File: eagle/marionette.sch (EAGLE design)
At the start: 483 parts, among them J12 IDC_RECEPTACLE_20PIN-S9172-ND, J13 CONN_HEADER_JTAG, J2 SP3T Jumper Switch, J22 ZX62D-B-5P8, J3 IDC_RECEPTACLE_2X20-S9175-ND, J5 CON_COAX_PWR_PJ-047AH-NO_MILL, J8 IDC_RECEPTACLE_2X20-S9175-ND, J9 IDC_RECEPTACLE_2X20-S9175-ND, M5002 IRFR9024NTRPBF, Q2 NFET_DUAL_DMN63D8LDW, Q3 AO3419, SW1 SW-MOM-TACTILE-B3F-1000, SW2 SW-MOM-TACTILE-B3F-1000, U1 SWITCH_74HC4066D, U10 LMV344, U11 STM32F427-STM32F427, U13 CON_HIROSE_DM3D(MICROSD), U14 USB3320, U15 SWITCH_74HC4066D, U17 LM3671, U2 FR014H5JZ, U3 MIC5305_MIC5305-3.3YD5, U4 DAC124S085CIMM, U40 MIC5305_MIC5305-3.3YD5, U41 MIC5305-MIC5305-1.8YD5, U5 MAX3051ESAESA+, U5002 TPS40200, U6 OPAMP_DUAL_MC4558CDT, U7 LMV344, U8 LMV344, U9 LMV344, X1 ABSO7

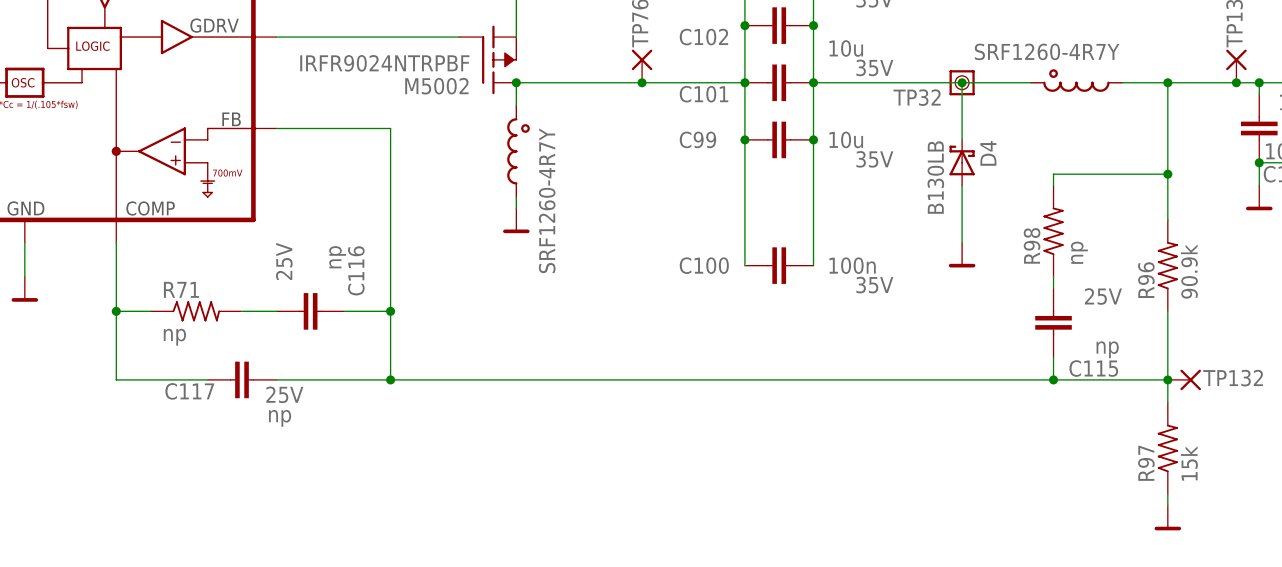
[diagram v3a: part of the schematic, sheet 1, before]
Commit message: Added compensation values to the marionette zeta.
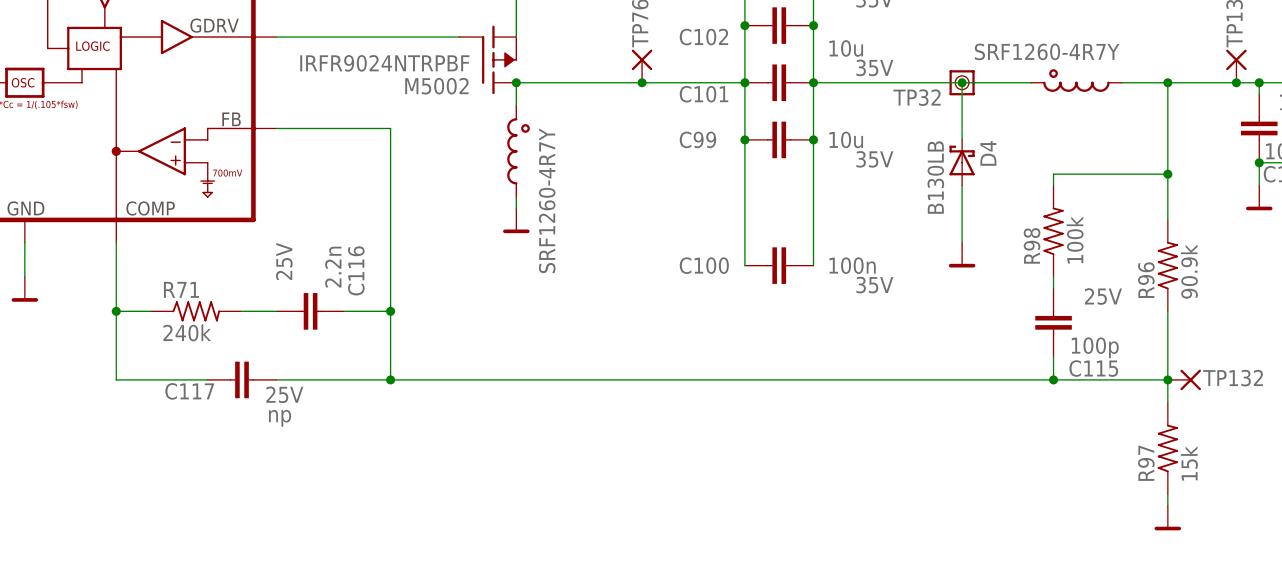
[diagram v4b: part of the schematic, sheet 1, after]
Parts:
- C115: value np -> 100p
- C116: value np -> 2.2n
- R71: value np -> 240k
- R98: value np -> 100k
- renumbered R1 to R201, R2 to R202, R3 to R203, R4 to R204
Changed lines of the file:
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@@
 <setting verticaltext="up"/>
 </settings>
-<grid distance="0.05" unitdist="inch" unit="inch" style="lines" multiple="2" display="no" altdistance="0.01" altunitdist="inch" altunit="inch"/>
+<grid distance="0.1" unitdist="inch" unit="inch" style="lines" multiple="1" display="no" altdistance="0.01" altunitdist="inch" altunit="inch"/>
 <layers>
 <layer number="1" name="Top" color="4" fill="1" visible="no" active="no"/>
@@
 <attribute name="V_RATING" value="10V"/>
 </part>
-<part name="R1" library="rcl_custom" deviceset="R-US_" device="0402-B" value="8.06k"/>
+<part name="R201" library="rcl_custom" deviceset="R-US_" device="0402-B" value="8.06k"/>
 <part name="C29" library="rcl_custom" deviceset="C-EU" device="0402-B" value="10n">
 <attribute name="V_RATING" value="10V"/>
@@
 <part name="GND3" library="GROUND" deviceset="GND" device=""/>
 <part name="J22" library="con-hirose-microusb" deviceset="ZX62D-B-5P8" device=""/>
-<part name="R2" library="rcl_custom" deviceset="R-US_" device="0402-B" value="4.7k"/>
-<part name="R3" library="rcl_custom" deviceset="R-US_" device="0402-B" value="4.7k"/>
+<part name="R202" library="rcl_custom" deviceset="R-US_" device="0402-B" value="4.7k"/>
+<part name="R203" library="rcl_custom" deviceset="R-US_" device="0402-B" value="4.7k"/>
 <part name="R6" library="rcl_custom" deviceset="R-US_" device="0402-B" value="4.7k"/>
 <part name="R7" library="rcl_custom" deviceset="R-US_" device="0402-B" value="4.7k"/>
@@
 <part name="TP119" library="marionette" deviceset="PAD+X" device="-0.7-NO_CREAM+SILK"/>
 <part name="TP120" library="marionette" deviceset="PAD+X" device="-0.7-NO_CREAM+SILK"/>
-<part name="R4" library="rcl_custom" deviceset="R-US_" device="0402-B" value="1Meg"/>
+<part name="R204" library="rcl_custom" deviceset="R-US_" device="0402-B" value="1Meg"/>
 <part name="C28" library="rcl_custom" deviceset="C-EU" device="0402-B" value="1u">
 <attribute name="V_RATING" value="10V"/>
@@
 <attribute name="V_RATING" value="10V"/>
 </part>
-<part name="C115" library="rcl_custom" deviceset="C-EU" device="0402-B" value="np">
+<part name="C115" library="rcl_custom" deviceset="C-EU" device="0402-B" value="100p">
 <attribute name="V_RATING" value="25V"/>
 </part>
-<part name="C116" library="rcl_custom" deviceset="C-EU" device="0402-B" value="np">
+<part name="C116" library="rcl_custom" deviceset="C-EU" device="0402-B" value="2.2n">
 <attribute name="V_RATING" value="25V"/>
 </part>
@@
 <part name="SW2" library="marionette" deviceset="SW-MOM-TACTILE" device="-B3F-1000"/>
 <part name="J5" library="marionette" deviceset="CON_COAX_PWR_PJ-047AH" device="-NO_MILL"/>
-<part name="R71" library="rcl_custom" deviceset="R-US_" device="0402-B" value="np"/>
+<part name="R71" library="rcl_custom" deviceset="R-US_" device="0402-B" value="240k"/>
 <part name="R96" library="rcl_custom" deviceset="R-US_" device="0402-B" value="90.9k"/>
 <part name="R97" library="rcl_custom" deviceset="R-US_" device="0402-B" value="15k"/>
-<part name="R98" library="rcl_custom" deviceset="R-US_" device="0402-B" value="np"/>
+<part name="R98" library="rcl_custom" deviceset="R-US_" device="0402-B" value="100k"/>
 <part name="C144" library="rcl_custom" deviceset="C-EU" device="0402-B" value="100p">
 <attribute name="V_RATING" value="50V"/>
@@
 </plain>
 <instances>
-<instance part="R1" gate="R" x="523.24" y="736.6" rot="R270"/>
+<instance part="R201" gate="R" x="523.24" y="736.6" rot="R270"/>
 <instance part="C29" gate="CE" x="427.99" y="803.91" smashed="yes">
 <attribute name="V_RATING" x="429.26" y="798.83" size="1.778" layer="96"/>
@@
 <instance part="FRAME1" gate="G$1" x="558.8" y="50.8"/>
 <instance part="FRAME1" gate="G$2" x="1010.92" y="0"/>
-<instance part="R2" gate="R" x="213.36" y="466.09" rot="R90"/>
-<instance part="R3" gate="R" x="226.06" y="466.09" rot="R90"/>
+<instance part="R202" gate="R" x="213.36" y="466.09" rot="R90"/>
+<instance part="R203" gate="R" x="226.06" y="466.09" rot="R90"/>
 <instance part="C34" gate="CE" x="251.46" y="350.52" smashed="yes" rot="R90">
 <attribute name="V_RATING" x="247.65" y="345.44" size="1.778" layer="96"/>
@@
 <attribute name="VALUE" x="247.142" y="26.543" size="0.762" layer="96" rot="R90"/>
 </instance>
-<instance part="R4" gate="R" x="646.43" y="742.95" smashed="yes" rot="R270">
+<instance part="R204" gate="R" x="646.43" y="742.95" smashed="yes" rot="R270">
 <attribute name="NAME" x="644.9314" y="736.6" size="1.778" layer="95" rot="R90"/>
 <attribute name="VALUE" x="643.128" y="749.3" size="1.778" layer="96" rot="R270"/>
@@
 <wire x1="641.35" y1="735.33" x2="646.43" y2="735.33" width="0.1524" layer="91"/>
 <junction x="652.78" y="735.33"/>
-<pinref part="R4" gate="R" pin="2"/>
+<pinref part="R204" gate="R" pin="2"/>
 <wire x1="646.43" y1="735.33" x2="652.78" y2="735.33" width="0.1524" layer="91"/>
 <wire x1="646.43" y1="735.33" x2="646.43" y2="737.87" width="0.1524" layer="91"/>
@@
 </segment>
 <segment>
-<pinref part="R1" gate="R" pin="2"/>
+<pinref part="R201" gate="R" pin="2"/>
 <wire x1="523.24" y1="731.52" x2="523.24" y2="730.25" width="0.1524" layer="91"/>
 <wire x1="523.24" y1="730.25" x2="525.78" y2="730.25" width="0.1524" layer="91"/>
@@
 <wire x1="652.78" y1="749.3" x2="652.78" y2="746.76" width="0.1524" layer="91"/>
 <junction x="652.78" y="749.3"/>
-<pinref part="R4" gate="R" pin="1"/>
+<pinref part="R204" gate="R" pin="1"/>
 <wire x1="646.43" y1="748.03" x2="646.43" y2="749.3" width="0.1524" layer="91"/>
 <wire x1="646.43" y1="749.3" x2="652.78" y2="749.3" width="0.1524" layer="91"/>
@@
 <segment>
 <pinref part="U14" gate="U" pin="RBIAS"/>
-<pinref part="R1" gate="R" pin="1"/>
+<pinref part="R201" gate="R" pin="1"/>
 <wire x1="523.24" y1="744.22" x2="523.24" y2="742.95" width="0.1524" layer="91"/>
 <pinref part="TP21" gate="TP" pin="P"/>
@@
 <wire x1="252.73" y1="459.74" x2="236.22" y2="459.74" width="0.1524" layer="91"/>
 <label x="132.08" y="459.74" size="1.778" layer="95" font="vector"/>
-<pinref part="R2" gate="R" pin="1"/>
+<pinref part="R202" gate="R" pin="1"/>
 <wire x1="236.22" y1="459.74" x2="213.36" y2="459.74" width="0.1524" layer="91"/>
 <wire x1="213.36" y1="459.74" x2="104.14" y2="459.74" width="0.1524" layer="91"/>
@@
 <wire x1="226.06" y1="454.66" x2="226.06" y2="461.01" width="0.1524" layer="91"/>
 <junction x="226.06" y="454.66"/>
-<pinref part="R3" gate="R" pin="1"/>
+<pinref part="R203" gate="R" pin="1"/>
 <pinref part="U11" gate="G6" pin="PF1"/>
 <pinref part="TP46" gate="TP" pin="P"/>
@@
 </segment>
 <segment>
-<pinref part="R2" gate="R" pin="2"/>
+<pinref part="R202" gate="R" pin="2"/>
 <wire x1="213.36" y1="471.17" x2="213.36" y2="472.44" width="0.1524" layer="91"/>
 <wire x1="213.36" y1="472.44" x2="226.06" y2="472.44" width="0.1524" layer="91"/>
-<pinref part="R3" gate="R" pin="2"/>
+<pinref part="R203" gate="R" pin="2"/>
 <wire x1="226.06" y1="472.44" x2="226.06" y2="471.17" width="0.1524" layer="91"/>
 <wire x1="226.06" y1="472.44" x2="226.06" y2="473.71" width="0.1524" layer="91"/>

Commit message: Added some datasheets and made some notes to the marionette.sch and marionette.brd
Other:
- note added: "Add power supply indicator lights, i.e. 5V, 3.3V_digital, 3.3V_analog, etc."
- note added: "Add some package details to MAX3051 SO-8 package: tplace layer demarcation of pin 1 Digikey part no. in the device info."
- note added: "This RGB LED is WAYYYY too small - get bigger package."
- note added: "Use ADP160AUJZ-1.8"
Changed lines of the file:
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@@
 <text x="1101.09" y="5.08" size="5.08" layer="94">2.0</text>
 <text x="1026.16" y="24.13" size="7.62" layer="94">POWER</text>
-<text x="861.06" y="276.86" size="7.62" layer="112">MIC5305 fixed regulators are non-stocked at Mouser and Digikey.  Also their accuracy is only 1%, so this was stupid choice.  Should use adjustable regulators for BOM reduction in future.</text>
-<text x="862.33" y="261.62" size="7.62" layer="112">Temporary fix for V2.0 is using the ADP121 1% LDO from Analog.</text>
+<text x="792.48" y="320.04" size="7.62" layer="112">MIC5305 fixed regulators are non-stocked at Mouser and Digikey.  Also their accuracy is only 1%, so this was stupid choice.  Should use adjustable regulators for BOM reduction in future.</text>
+<text x="791.21" y="304.8" size="7.62" layer="112">Temporary fix for V2.0 is using the ADP121 1% LDO from Analog.</text>
+<text x="726.44" y="236.22" size="1.778" layer="112">Use ADP160AUJZ-1.8</text>
+<text x="792.48" y="292.1" size="7.62" layer="112">Add power supply indicator lights, i.e. 5V, 3.3V_digital, 3.3V_analog, etc.</text>
 </plain>
 <instances>
@@
 The trace capacitance is about 1pF.
  Therefore choose parallel caps of 11pF.</text>
+<text x="180.34" y="500.38" size="5.08" layer="112">This RGB LED is WAYYYY too small
+- get bigger package.</text>
+<text x="960.12" y="662.94" size="5.08" layer="112">Add some package details to MAX3051 SO-8 package:
+tplace layer
+demarcation of pin 1
+Digikey part no. in the device info.</text>
 </plain>
 <instances>
